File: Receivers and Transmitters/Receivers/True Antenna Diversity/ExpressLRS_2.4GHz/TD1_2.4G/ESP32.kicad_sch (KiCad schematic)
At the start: 10 parts, among them U8 ESP32-PICO-D4

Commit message: Updated schematics for TD1_2.4G receiver: ESP32, SX1280, and RFX2401C blocks
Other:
- company: https://github.com/Paschalis | TeodoraMiu -> https://github.com/Paschalis
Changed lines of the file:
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@@
 		(date "2025-02-23")
 		(rev "1.0")
-		(company "https://github.com/Paschalis | TeodoraMiu")
+		(company "https://github.com/Paschalis")
 	)
 	(text "Paschalis M."
@@
 		(at 187.96 64.77 270)
 		(unit 1)
-		(exclude_from_sim yes)
+		(exclude_from_sim no)
 		(in_bom yes)
 		(on_board yes)

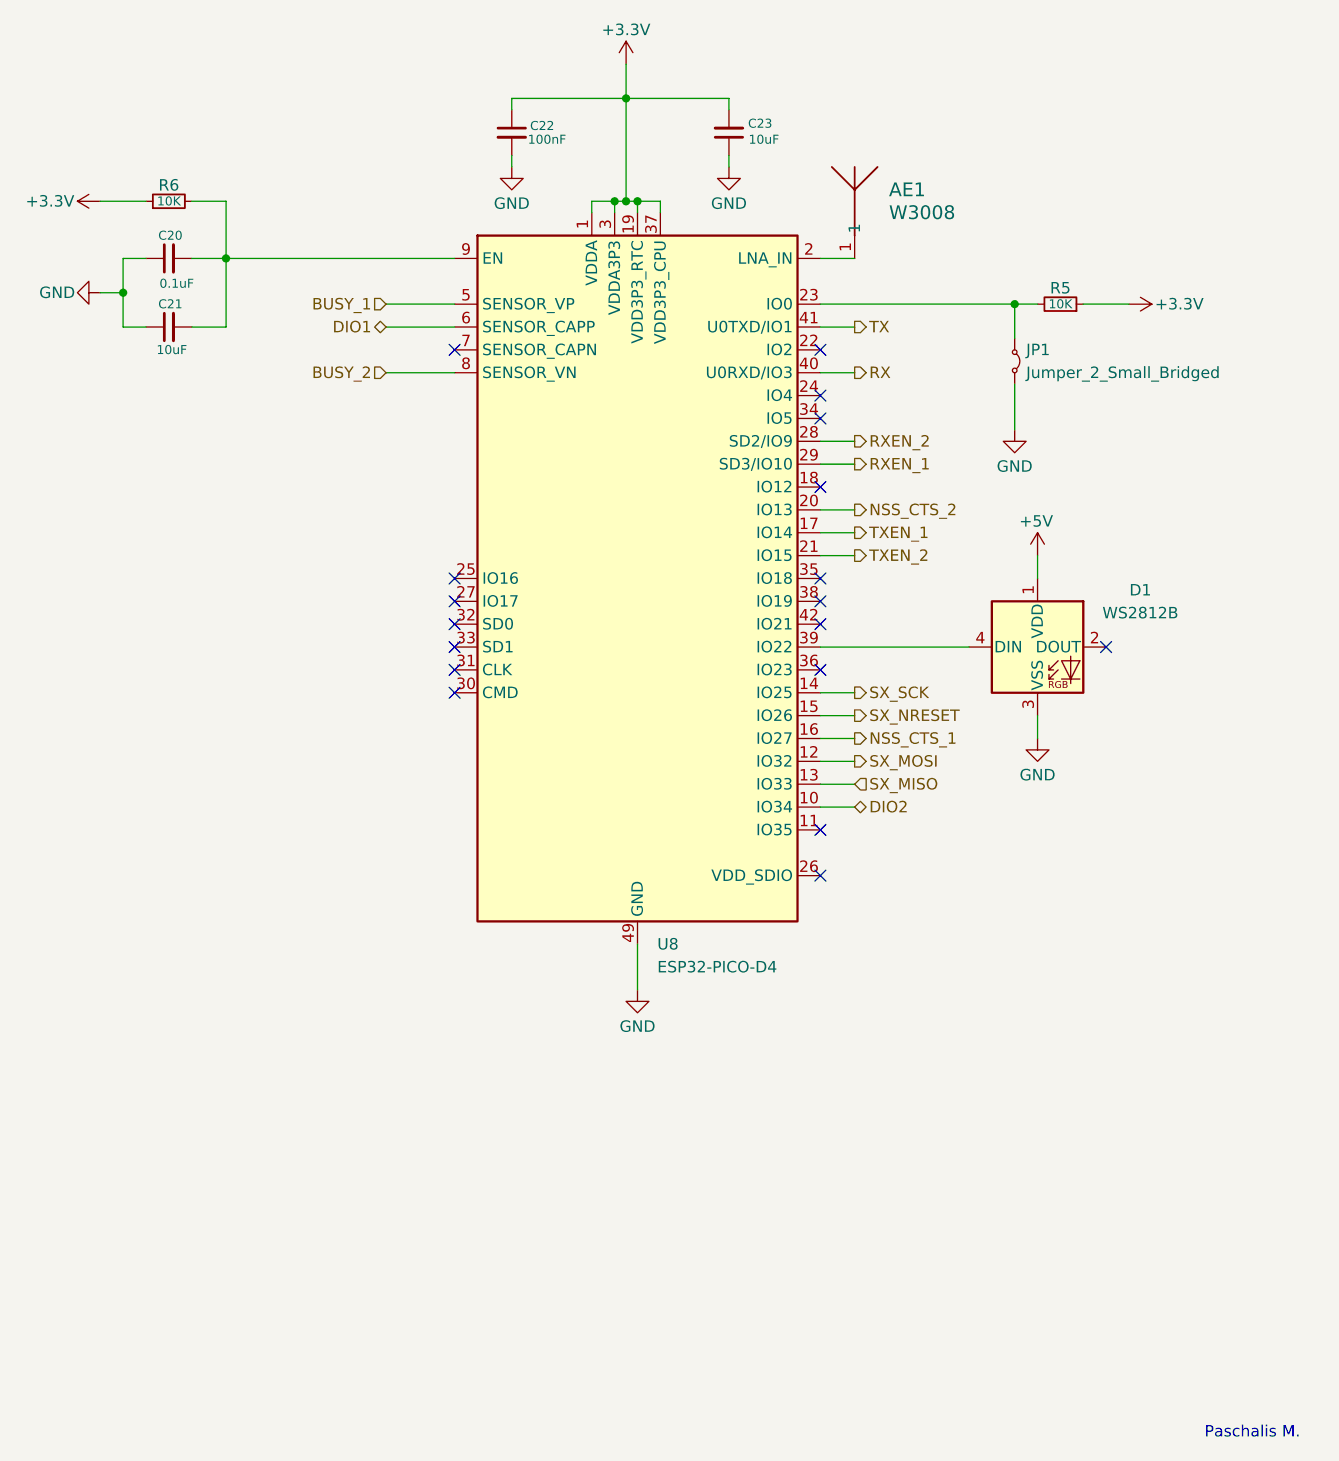
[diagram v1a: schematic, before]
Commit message: Update Antenna Diversity (AD1_2.4G), True Antenna Diversity (TD1_2.4G), and Gemini Mode transmitter (G_TX1): Modify KiCad files, add BOMs and production files; update images, docs, videos, and README; remove outdated Mechanical CAD file
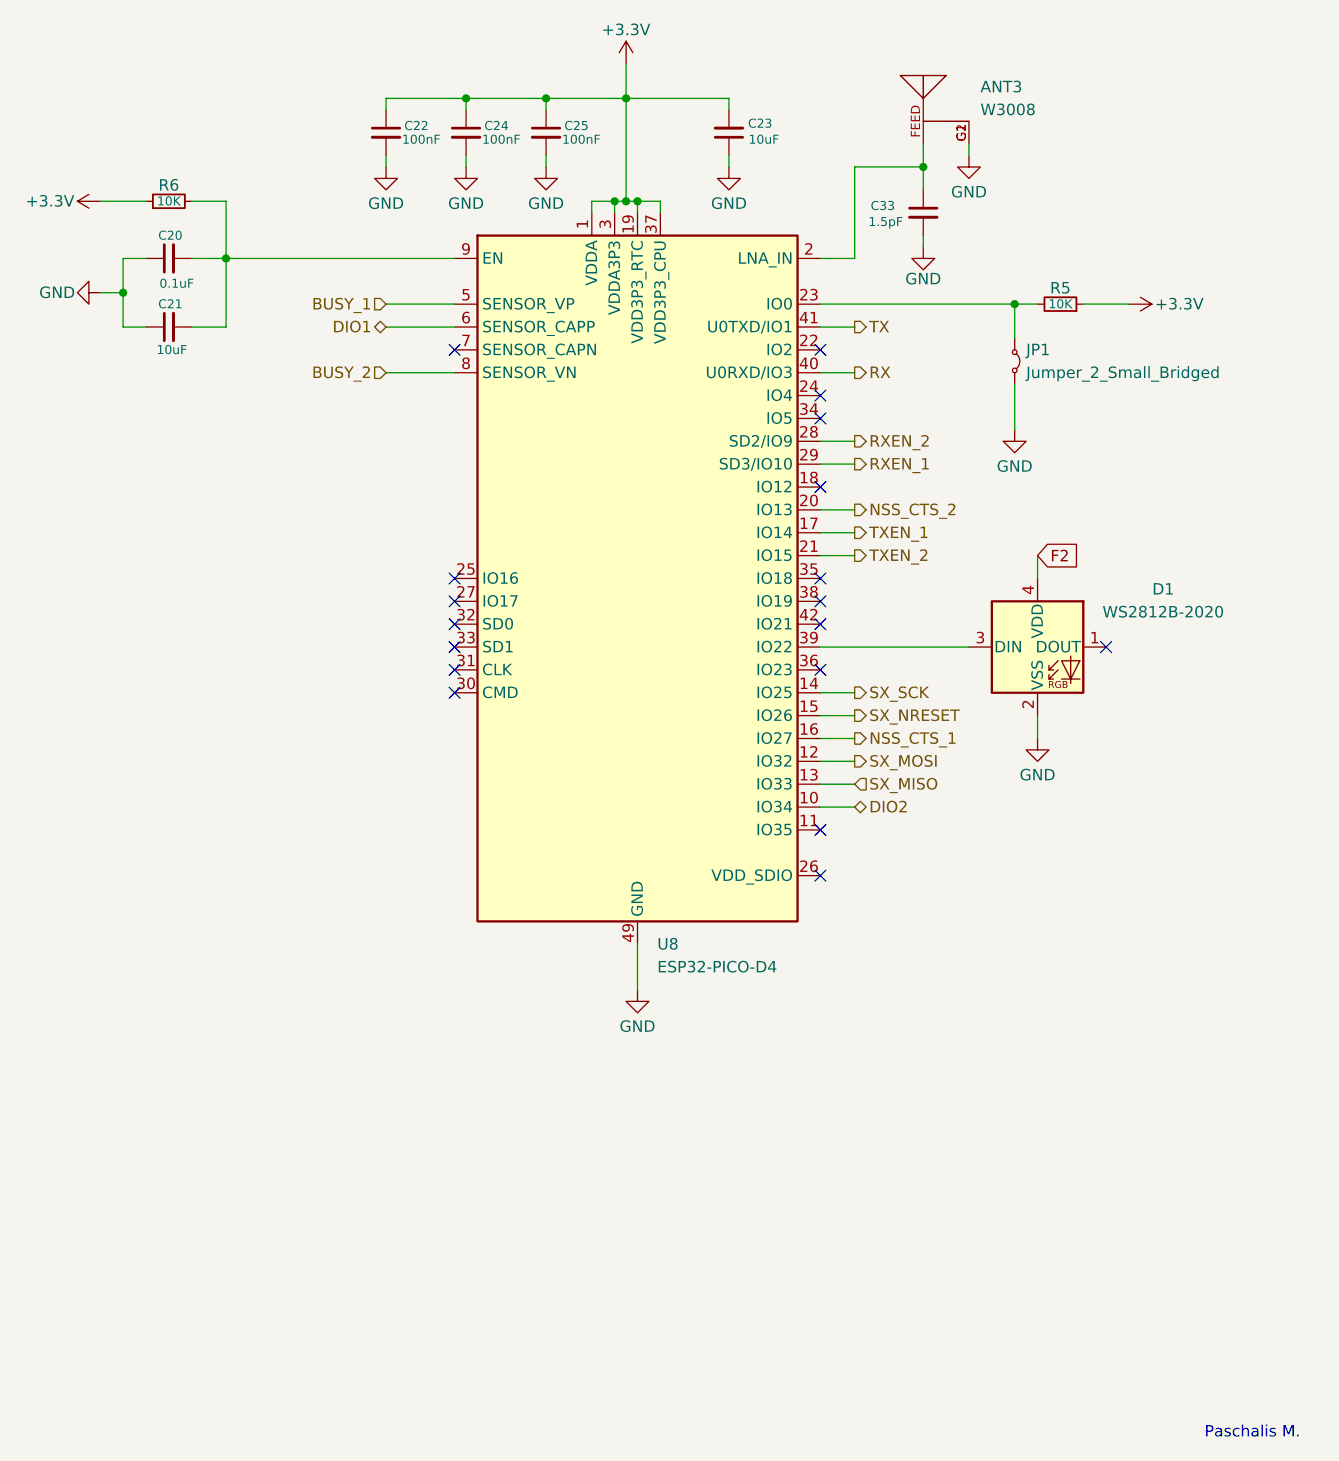
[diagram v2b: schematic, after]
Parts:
- removed AE1: W3008, W3008:ANT_W3008_PUL, symbol W3008:W3008
- removed D1: WS2812B, LED_SMD:LED_WS2812B_PLCC4_5.0x5.0mm_P3.2mm, symbol LED:WS2812B
- added ANT3: W3008, W3008:ANTENNA_W3008, symbol W3008:W3008
- added C24, C25: 100nF, Capacitor_SMD:C_0603_1608Metric_Pad1.08x0.95mm_HandSolder, symbol Device:C_Small
- added C33: 1.5pF, Capacitor_SMD:C_01005_0402Metric_Pad0.57x0.30mm_HandSolder, symbol Device:C_Small
- added D1: WS2812B-2020, LED_SMD:LED_WS2812B-2020_PLCC4_2.0x2.0mm, symbol LED:WS2812B-2020
- JP1: footprint TestPoint:TestPoint_2Pads_Pitch2.54mm_Drill0.8mm -> TestPoint:TestPoint_Bridge_Pitch2.0mm_Drill0.7mm
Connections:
- net +3.3V: now also C24.1, C25.1
- net GND: now also ANT3.G1, ANT3.G2, C24.2, C25.2, C33.2, D1.2 (VSS)
- net at U8.2 (LNA_IN): now also ANT3.FEED, C33.1
- net at U8.39 (IO22): now also D1.3 (DIN)
- new net F2: D1.4 (VDD)
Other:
- moved on the sheet: C22

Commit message: Update TD1_2.4G: schematic and PCB revisions, BOM export, README; remove old PCBWay production files
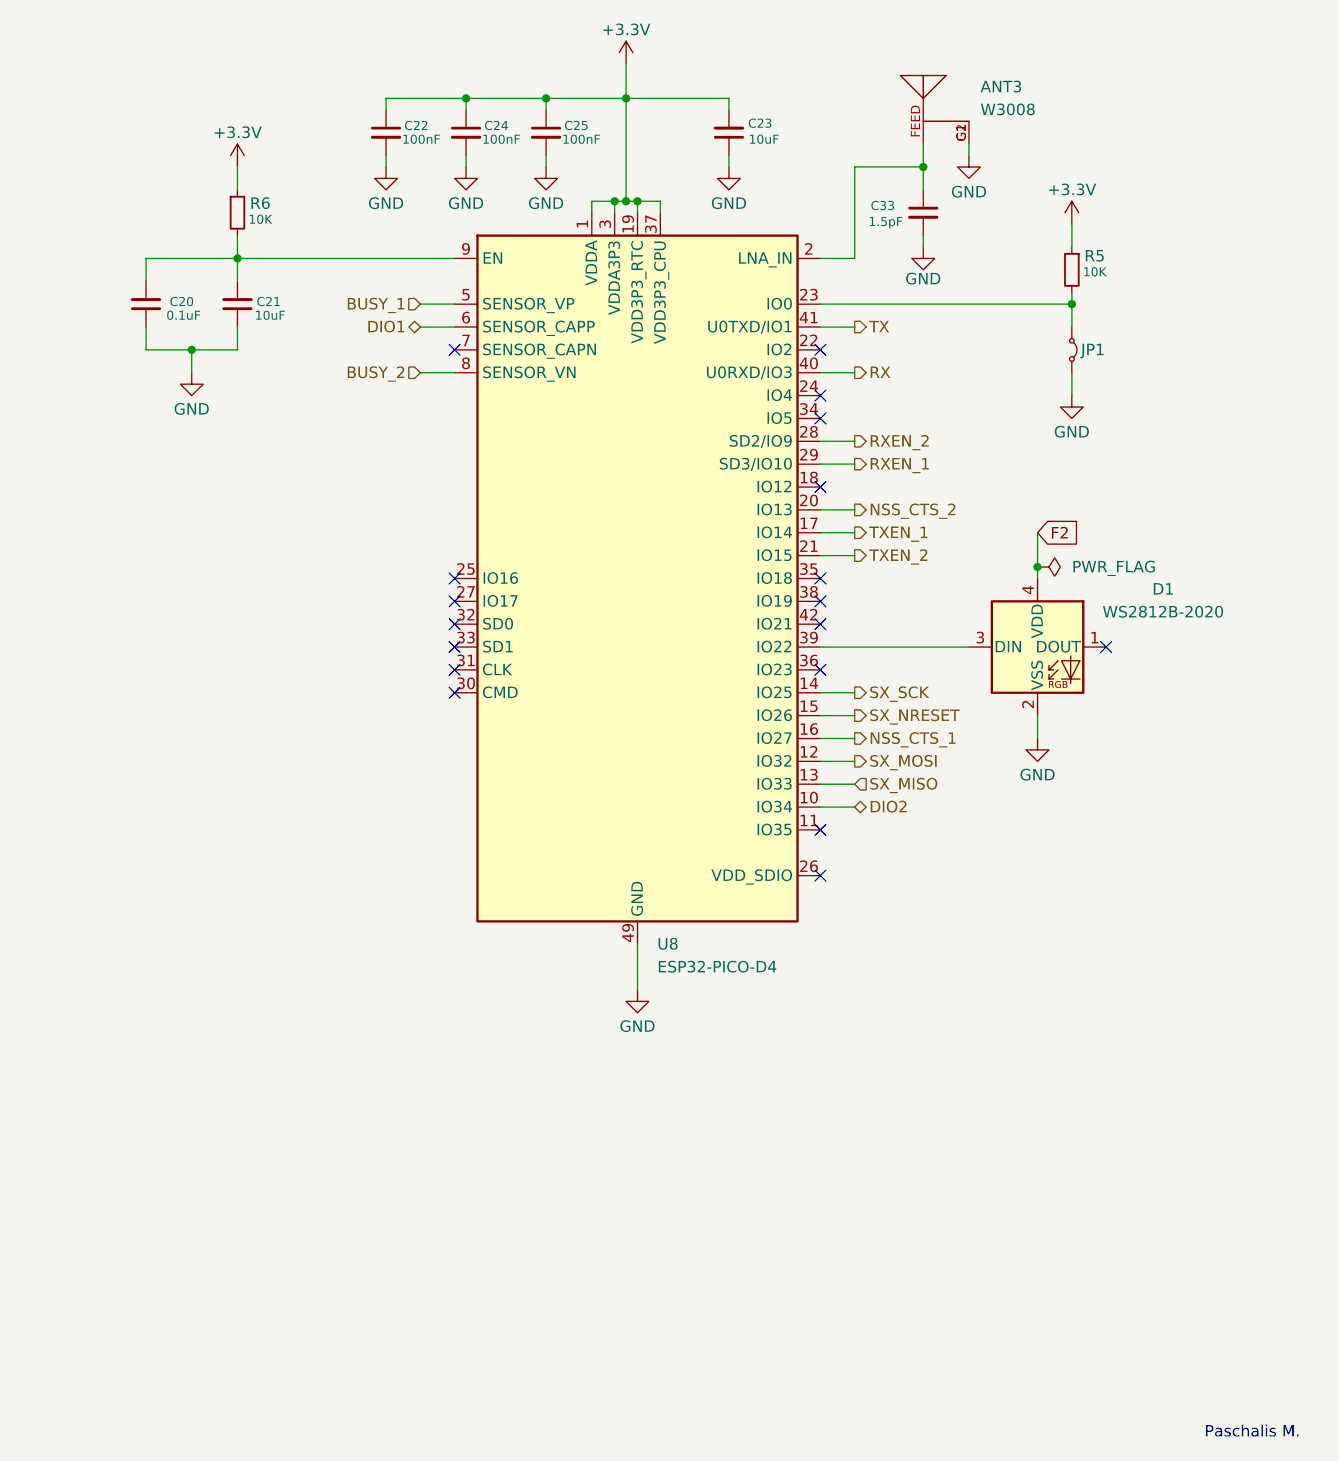
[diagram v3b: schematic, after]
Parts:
- JP1: footprint TestPoint:TestPoint_Bridge_Pitch2.0mm_Drill0.7mm -> TestPoint:TestPoint_2Pads_Pitch2.54mm_Drill0.8mm
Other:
- moved on the sheet: C20, C21, R5, R6
